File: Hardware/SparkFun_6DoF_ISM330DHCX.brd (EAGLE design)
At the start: 25.4 x 25.4 mm, 64 parts, among them J1 QWIIC_RIGHT_ANGLE, J2 QWIIC_RIGHT_ANGLE, U1 LSM6DS0

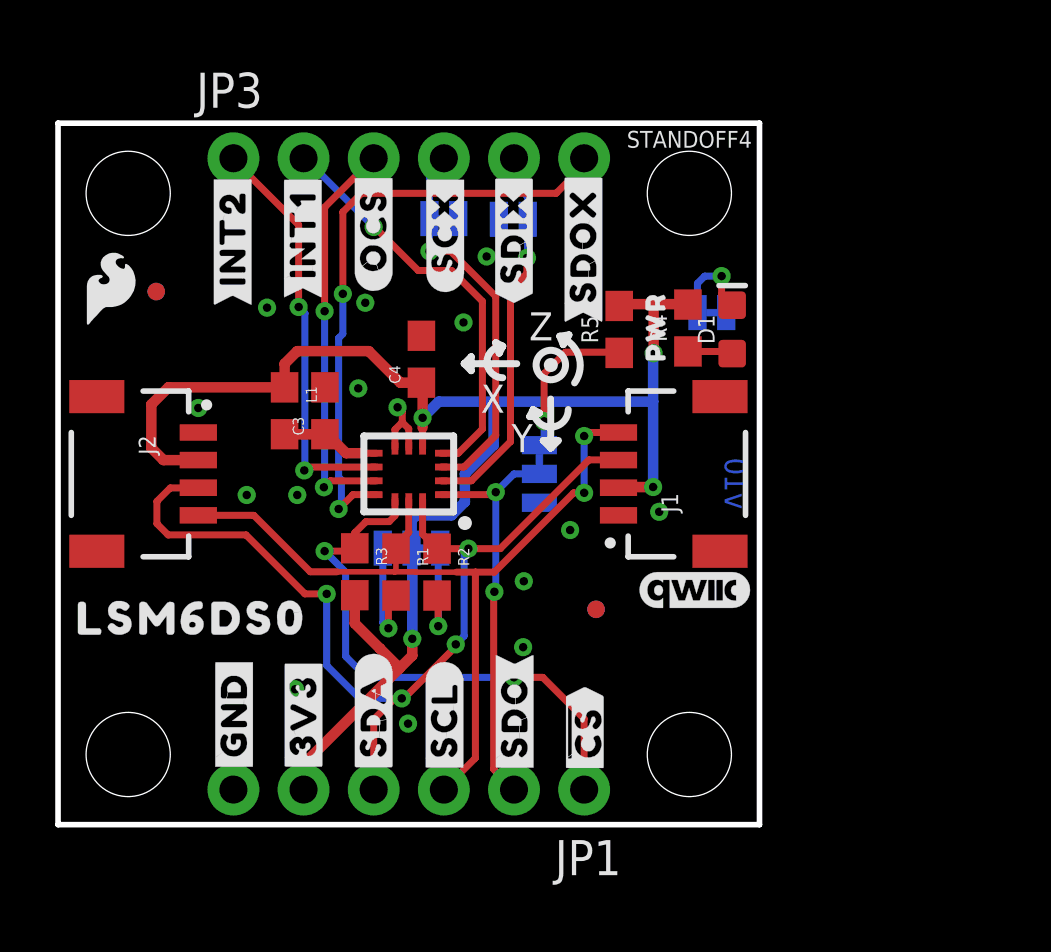
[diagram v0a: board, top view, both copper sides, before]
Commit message: Fixes IC name
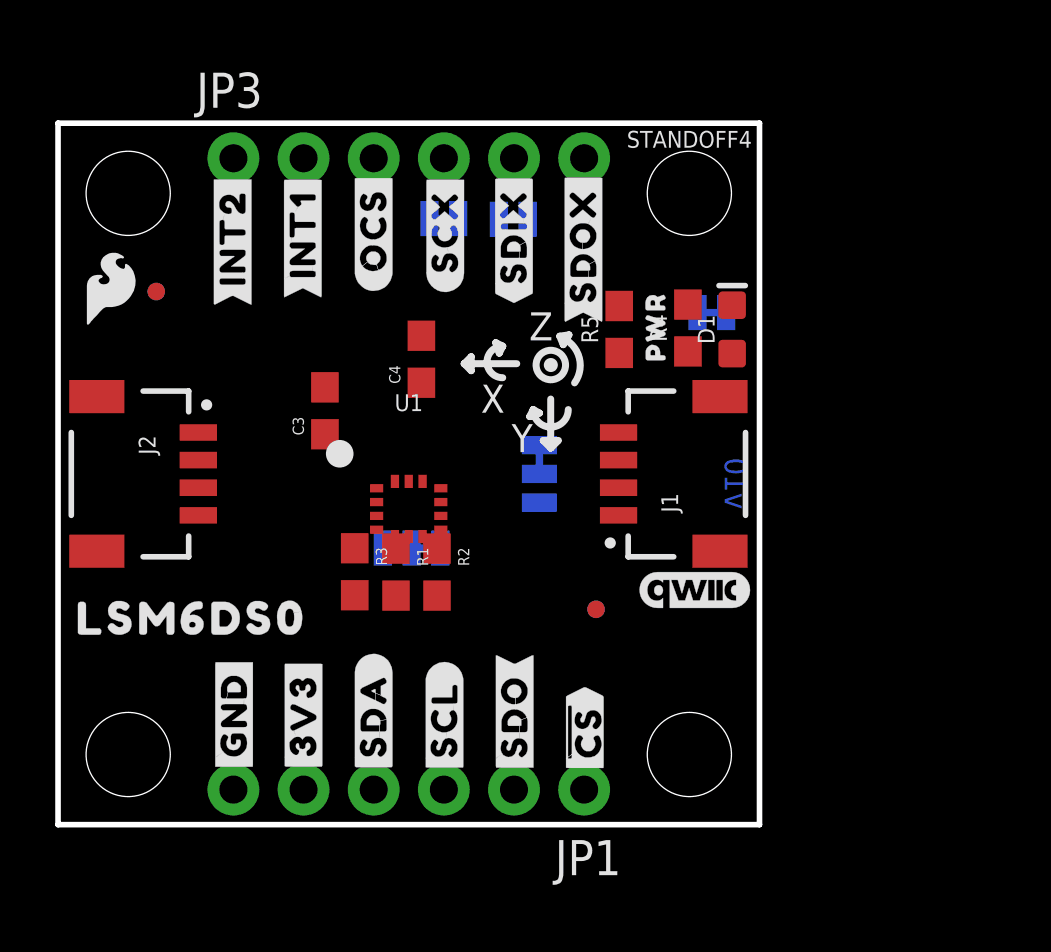
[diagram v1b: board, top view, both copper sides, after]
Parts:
- removed L1: 30Ω, SparkFun-Coils:0603
- U1: value LSM6DS0 -> ISM330DHCX; device temp:LGA14L -> ISM330DHCX:LGA-14L
- moved U1 1.27 mm to (12.7, 11.4), turned to 0 degrees
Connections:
- removed net VDD: C3.1, L1.2, U1.8
- new net N$4: C3.1, U1.P8
- new net SDX: U1.P2
- net !CS!: now also U1.P12; no longer U1.12
- net 3.3V: now also U1.P5; no longer L1.1, U1.5
- net GND: now also U1.P6, U1.P7; no longer U1.6, U1.7
- net INT1: now also U1.P4; no longer U1.4
- net INT2: now also U1.P9; no longer U1.9
- net OCS: now also U1.P10; no longer U1.10
- net SCL: now also U1.P13; no longer U1.13
- net SCX: now also U1.P3; no longer U1.3
- net SDA: now also U1.P14; no longer U1.14
- net SDI_AUX: no longer U1.2
- net SDO/SA0: now also U1.P1; no longer U1.1
- net SDO_AUX: now also U1.P11; no longer U1.11
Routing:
- net 3.3V: track 57.4 -> 0.00 mm, vias 4 -> 0
- net SDA: track 35.8 -> 0.00 mm, vias 4 -> 0
- net SCL: track 30.5 -> 0.00 mm, vias 2 -> 0
- net SDO_AUX: track 22.2 -> 0.00 mm, vias 2 -> 0
- net !CS!: track 20.3 -> 0.00 mm, vias 2 -> 0
- net INT2: track 15.1 -> 0.00 mm, vias 2 -> 0
- net INT1: track 15.1 -> 0.00 mm, vias 1 -> 0
- net SDO/SA0: track 15.0 -> 0.00 mm, vias 2 -> 0
- net OCS: track 14.7 -> 0.00 mm, vias 2 -> 0
- net SCX: track 14.1 -> 0.00 mm, vias 1 -> 0
- net SDI_AUX: track 13.8 -> 0.00 mm, vias 1 -> 0
- net N$1: track 5.71 -> 0.00 mm, vias 1 -> 0
- net N$5: track 4.28 -> 0.00 mm, vias 1 -> 0
- net N$6: track 3.98 -> 0.00 mm, vias 1 -> 0
- net VDD: track 3.82 -> 0.00 mm
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
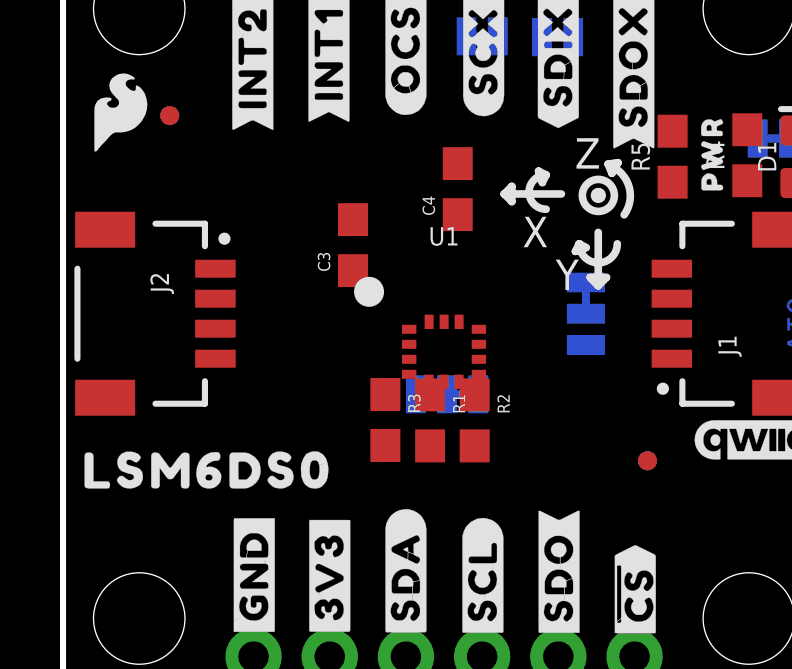
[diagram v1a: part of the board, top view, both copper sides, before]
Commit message: Updates notes in schematic (schematic done)
* Adds 10k to ground to address selection just in case someone bridges the entire three way jumper
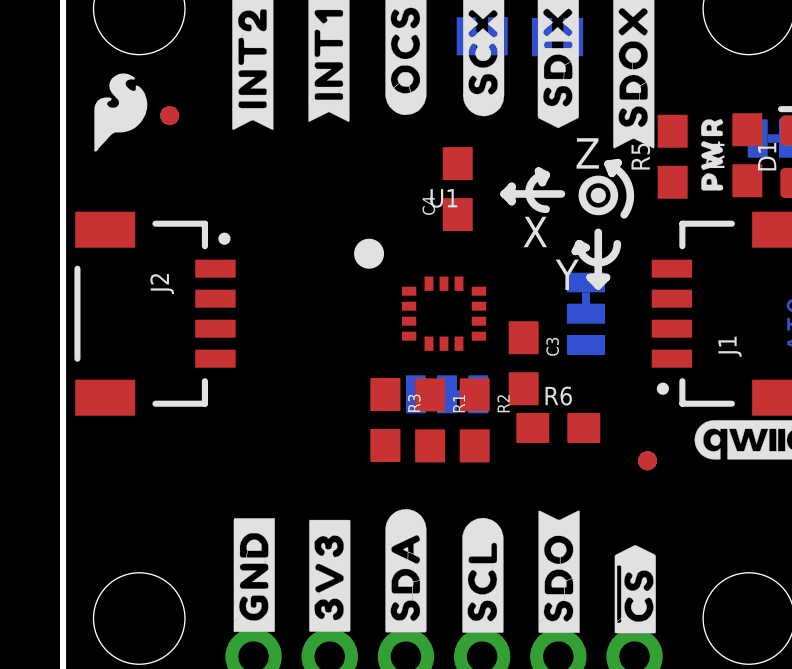
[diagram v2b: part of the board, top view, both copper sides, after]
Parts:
- removed U$12, U$30: (no value), top:LSM6DS011
- added R6: 10k, SparkFun-Resistors:0603
- R1, R2: value 4.7k -> 2.2k
- R5: value 100k -> 10k
- moved C3 6.92 mm to (15.4, 11.0), turned to 270 degrees
- moved U1 1.27 mm to (12.7, 12.7)
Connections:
- new net N$7: ADDR.1, R6.2
- net GND: now also R6.1; no longer ADDR.1

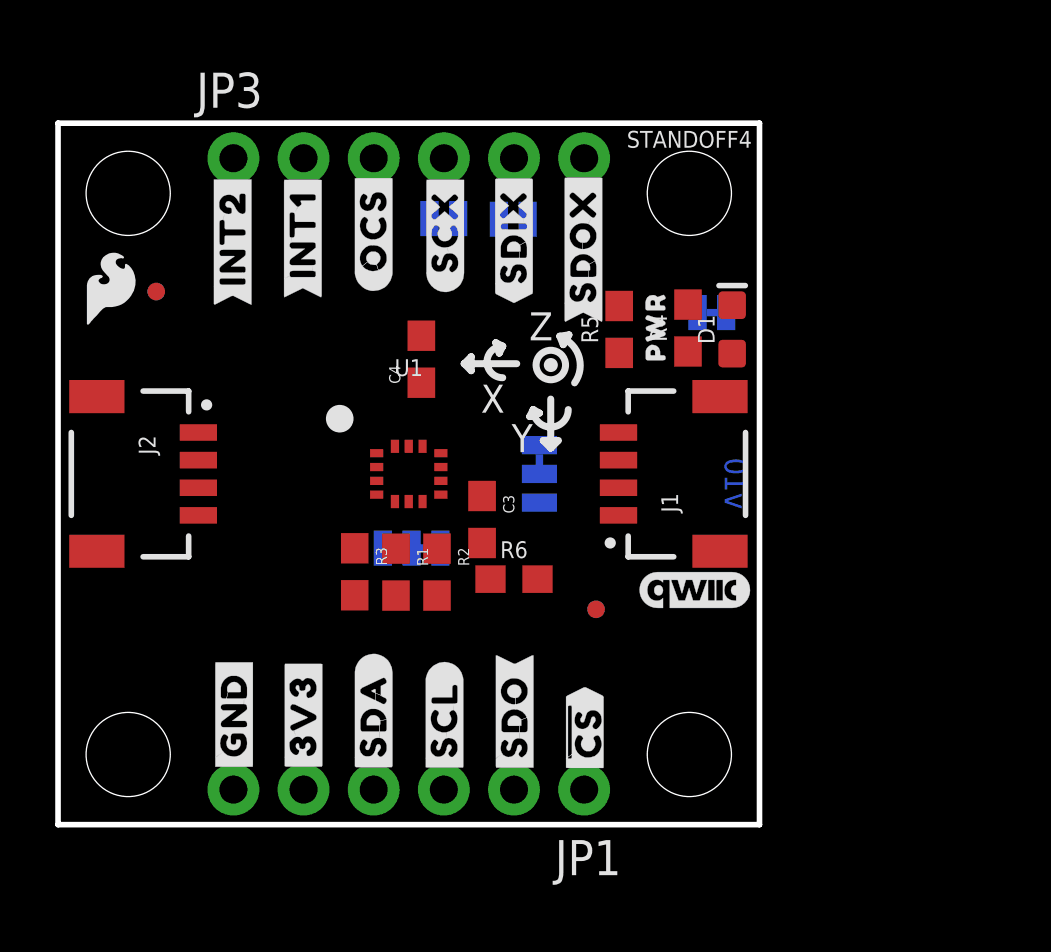
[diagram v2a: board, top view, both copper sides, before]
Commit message: Completes routing, had to swap SDO and CS for ease of routing
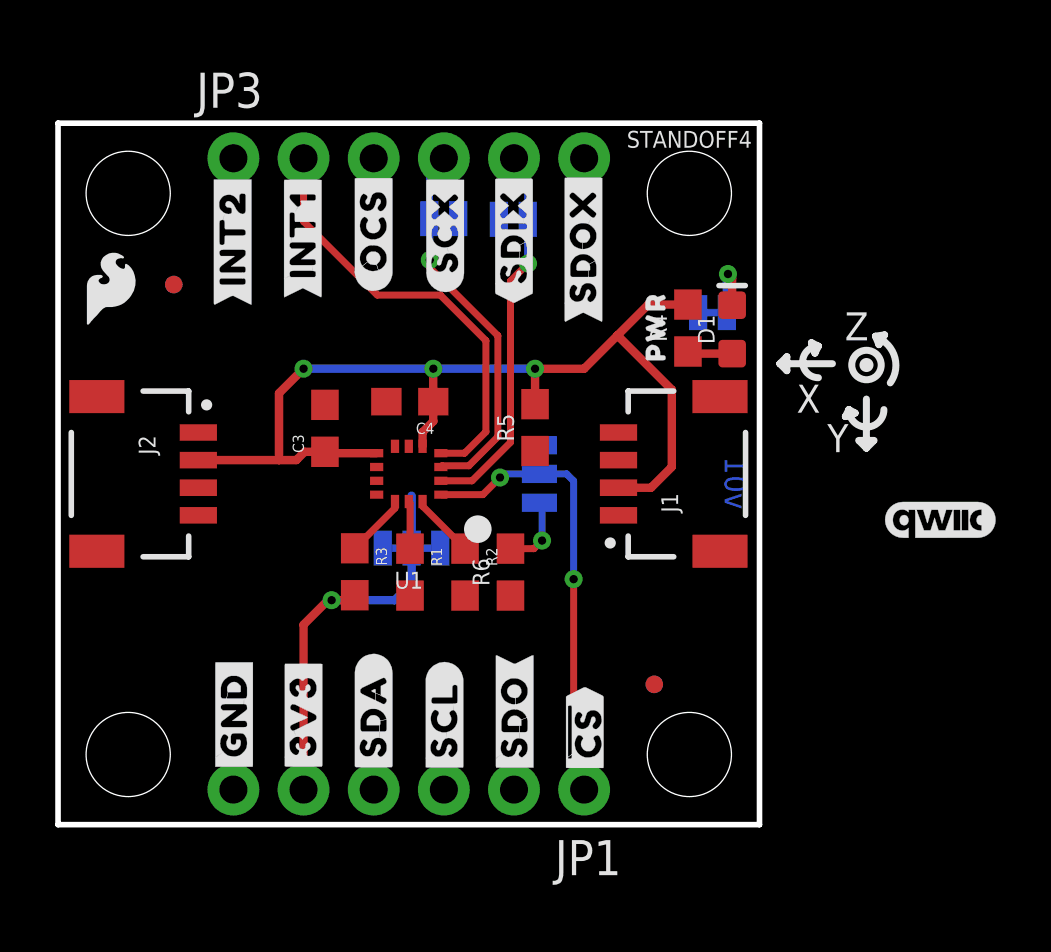
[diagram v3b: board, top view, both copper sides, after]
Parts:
- moved LOGO1 9.25 mm to (32.0, 11.0)
- moved C3 6.58 mm to (9.66, 14.4), turned to 90 degrees
- moved R5 4.68 mm to (17.3, 14.4)
- moved FD2 3.44 mm to (21.6, 5.08)
- moved FID2 3.44 mm to (21.6, 5.08)
- moved C4 1.59 mm to (12.7, 15.3), turned to 180 degrees
- moved R2 1.02 mm to (14.7, 9.14)
- moved FD1 0.68 mm to (4.19, 19.6)
- moved FID1 0.68 mm to (4.19, 19.6)
- moved R1 0.51 mm to (12.7, 9.14)
- moved R6 0.28 mm to (16.4, 9.14), turned to 90 degrees
- turned LED to 180 degrees
- turned U1 to 180 degrees
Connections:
- removed net N$4: C3.1, U1.P8
- removed net SDX: U1.P2
- net !CS!: now also JP1.2; no longer JP1.1
- net 3.3V: now also C3.1, U1.P8
- net SDI_AUX: now also U1.P2
- net SDO/SA0: now also JP1.1; no longer JP1.2
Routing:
- net 3.3V: track 0.00 -> 51.8 mm, vias 0 -> 4
- net INT1: track 0.00 -> 15.9 mm
- net SDI_AUX: track 0.00 -> 13.9 mm, vias 0 -> 1
- net SCX: track 0.00 -> 13.8 mm, vias 0 -> 1
- net SDO/SA0: track 0.00 -> 13.0 mm, vias 0 -> 2
- net N$7: track 0.00 -> 2.68 mm, vias 0 -> 1
- net N$3: track 0.00 -> 2.61 mm, vias 0 -> 1
- net SDA: track 0.00 -> 2.34 mm
- net !CS!: track 0.00 -> 2.30 mm
- net SCL: track 0.00 -> 1.72 mm
- net N$2: track 0.00 -> 1.63 mm
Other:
- board text added: "v01"
- board text removed: "v10"

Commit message: Adds labels, fixes wonky box in schematic
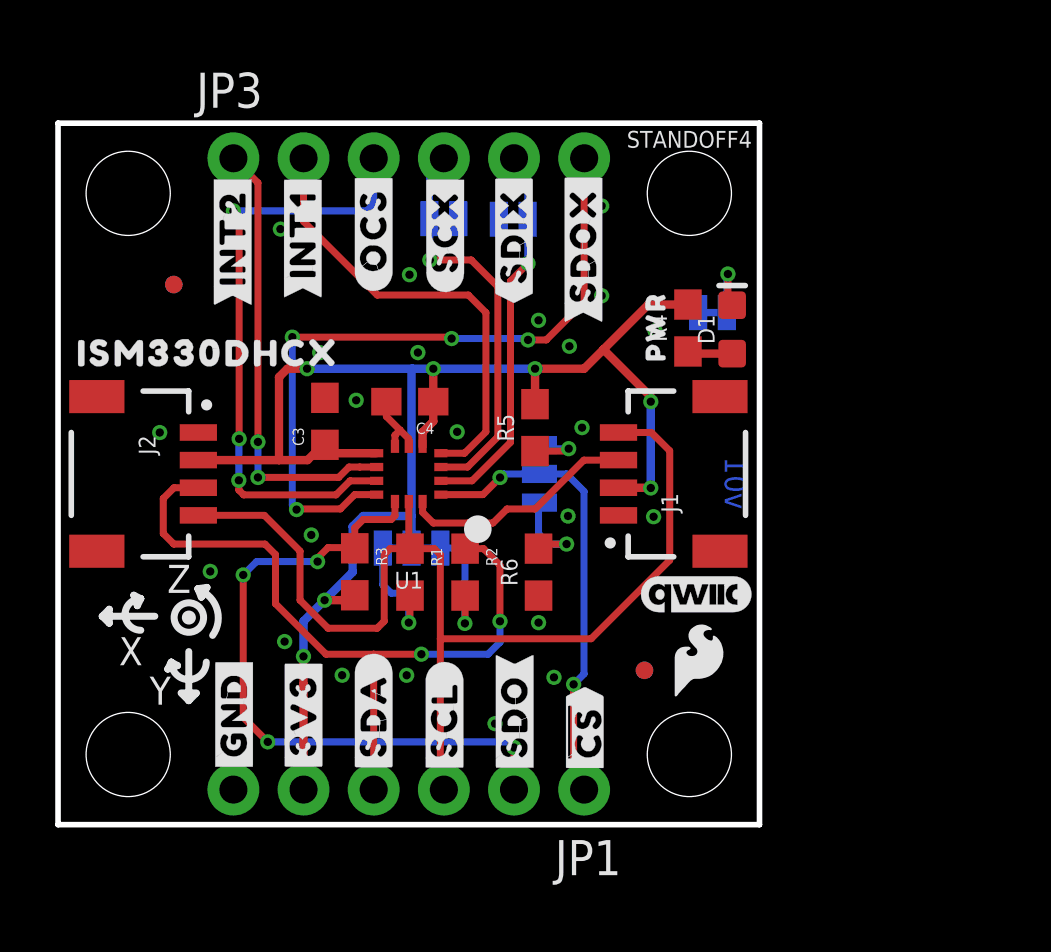
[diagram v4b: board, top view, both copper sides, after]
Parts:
- added U$12: (no value), ISMTop:ISM330DHCX331
- added U$30: (no value), ISMTop:ISM330DHCX20
- LOGO2: value OSHW-LOGOS -> OSHW-LOGOMINI; device SparkFun-Aesthetics:OSHW-LOGO-S -> SparkFun-Aesthetics:OSHW-LOGO-MINI
- moved U$29 25.2 mm to (23.2, 5.97)
- moved LOGO2 22.2 mm to (23.8, 14.7)
- moved LOGO1 9.24 mm to (23.1, 8.33)
- moved R6 1.02 mm to (17.4, 9.14)
- moved U$31 0.93 mm to (5.69, 12.9)
- moved FD2 0.62 mm to (21.2, 5.59)
- moved FID2 0.62 mm to (21.2, 5.59)
- moved C3 0.25 mm to (9.66, 14.6)
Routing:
- net SCL: track 1.72 -> 40.1 mm
- net SDA: track 2.34 -> 36.8 mm, vias 0 -> 2
- net SDO_AUX: track 0.00 -> 25.8 mm, vias 0 -> 4
- net OCS: track 0.00 -> 22.3 mm, vias 0 -> 3
- net !CS!: track 2.30 -> 24.4 mm, vias 0 -> 4
- net INT2: track 0.00 -> 16.4 mm, vias 0 -> 2
- net 3.3V: track 51.8 -> 57.1 mm, vias 4 -> 7
- net N$6: track 0.00 -> 4.49 mm, vias 0 -> 1
- net N$5: track 0.00 -> 4.38 mm, vias 0 -> 1
- net SDO/SA0: track 13.0 -> 16.9 mm
- net GND: track 0.00 -> 2.62 mm, vias 0 -> 23
- net N$1: track 0.00 -> 2.37 mm, vias 0 -> 1
- net SCX: track 13.8 -> 14.7 mm
- net N$7: track 2.68 -> 3.47 mm
- net INT1: track 15.9 -> 16.5 mm
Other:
- board text removed: "Revised By: Elias Santistevan"
